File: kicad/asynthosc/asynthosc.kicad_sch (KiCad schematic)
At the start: 14 parts

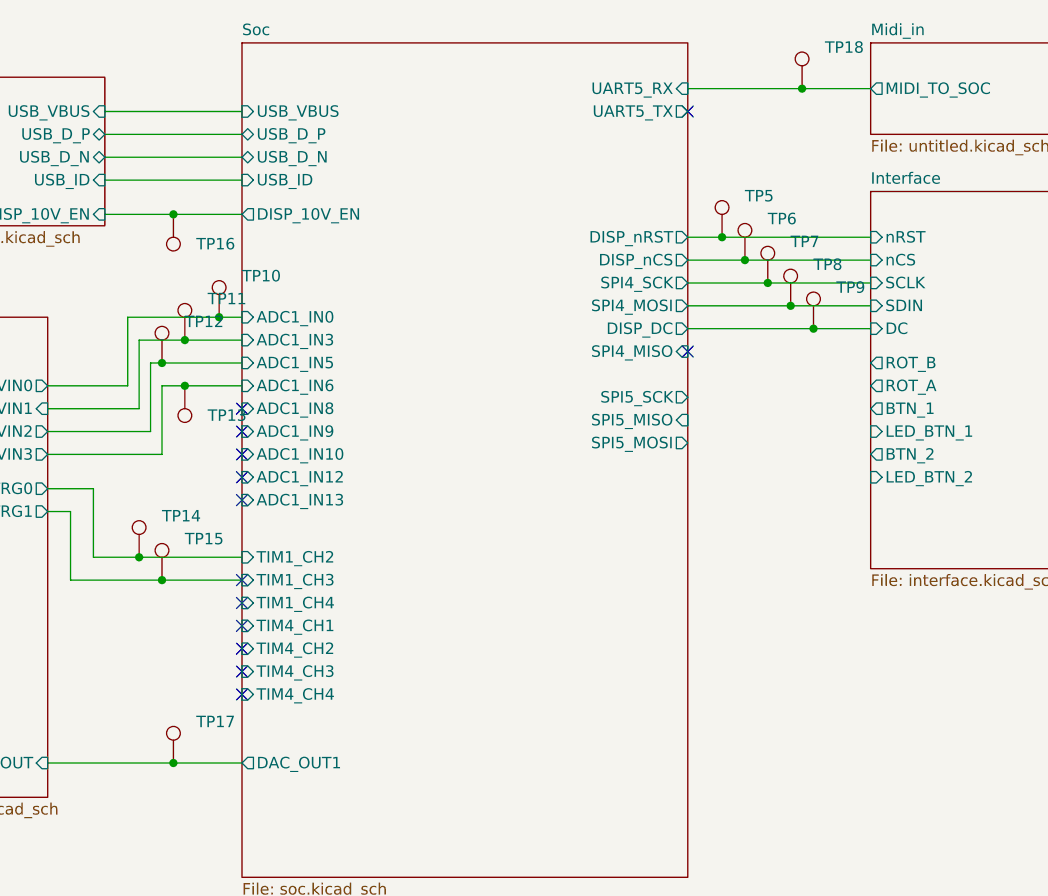
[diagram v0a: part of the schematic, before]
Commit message: pcb: place and change some components for easier routing
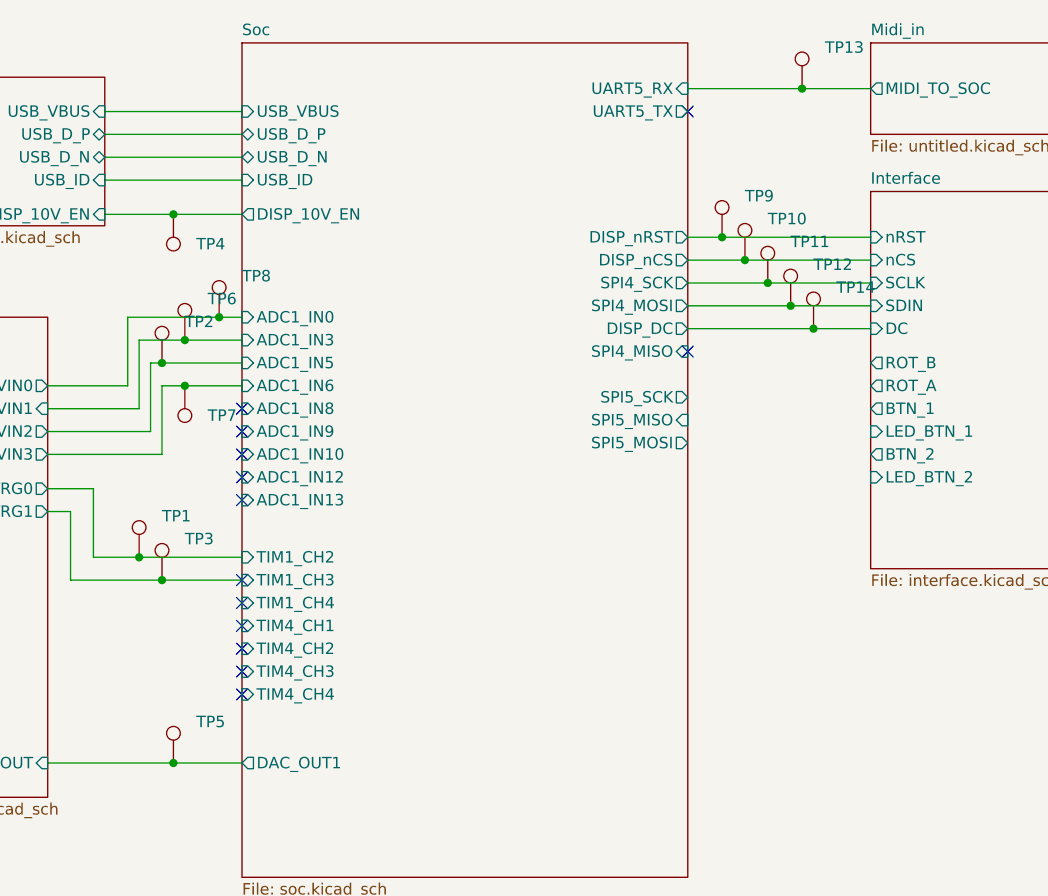
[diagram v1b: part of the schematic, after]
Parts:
- renumbered TP14 to TP1, TP6 to TP10, TP7 to TP11, TP8 to TP12, TP18 to TP13, TP9 to TP14, TP12 to TP2, TP15 to TP3, TP16 to TP4, TP17 to TP5, TP11 to TP6, TP13 to TP7, TP10 to TP8, TP5 to TP9
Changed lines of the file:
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@@
 		(dnp no)
 		(fields_autoplaced yes)
-		(property "Reference" "TP10"
+		(property "Reference" "TP8"
 			(at 127 97.0279 0)
 			(effects
@@
 			(project "asynthosc"
 				(path "/d73e377a-a016-415f-8824-91cc6e4907b9"
-					(reference "TP10")
+					(reference "TP8")
 					(unit 1)
 				)
@@
 		(dnp no)
 		(fields_autoplaced yes)
-		(property "Reference" "TP8"
+		(property "Reference" "TP12"
 			(at 190.5 95.7579 0)
 			(effects
@@
 			(project "asynthosc"
 				(path "/d73e377a-a016-415f-8824-91cc6e4907b9"
-					(reference "TP8")
+					(reference "TP12")
 					(unit 1)
 				)
@@
 		(dnp no)
 		(fields_autoplaced yes)
-		(property "Reference" "TP7"
+		(property "Reference" "TP11"
 			(at 187.96 93.2179 0)
 			(effects
@@
 			(project "asynthosc"
 				(path "/d73e377a-a016-415f-8824-91cc6e4907b9"
-					(reference "TP7")
+					(reference "TP11")
 					(unit 1)
 				)
@@
 		(dnp no)
 		(fields_autoplaced yes)
-		(property "Reference" "TP15"
+		(property "Reference" "TP3"
 			(at 120.65 126.2379 0)
 			(effects
@@
 			(project "asynthosc"
 				(path "/d73e377a-a016-415f-8824-91cc6e4907b9"
-					(reference "TP15")
+					(reference "TP3")
 					(unit 1)
 				)
@@
 		(dnp no)
 		(fields_autoplaced yes)
-		(property "Reference" "TP14"
+		(property "Reference" "TP1"
 			(at 118.11 123.6979 0)
 			(effects
@@
 			(project "asynthosc"
 				(path "/d73e377a-a016-415f-8824-91cc6e4907b9"
-					(reference "TP14")
+					(reference "TP1")
 					(unit 1)
 				)
@@
 		(dnp no)
 		(fields_autoplaced yes)
-		(property "Reference" "TP17"
+		(property "Reference" "TP5"
 			(at 121.92 146.5579 0)
 			(effects
@@
 			(project "asynthosc"
 				(path "/d73e377a-a016-415f-8824-91cc6e4907b9"
-					(reference "TP17")
+					(reference "TP5")
 					(unit 1)
 				)
@@
 		(dnp no)
 		(fields_autoplaced yes)
-		(property "Reference" "TP13"
+		(property "Reference" "TP7"
 			(at 123.19 112.5219 0)
 			(effects
@@
 			(project "asynthosc"
 				(path "/d73e377a-a016-415f-8824-91cc6e4907b9"
-					(reference "TP13")
+					(reference "TP7")
 					(unit 1)
 				)
@@
 		(dnp no)
 		(fields_autoplaced yes)
-		(property "Reference" "TP16"
+		(property "Reference" "TP4"
 			(at 121.92 93.4719 0)
 			(effects
@@
 			(project "asynthosc"
 				(path "/d73e377a-a016-415f-8824-91cc6e4907b9"
-					(reference "TP16")
+					(reference "TP4")
 					(unit 1)
 				)
@@
 		(dnp no)
 		(fields_autoplaced yes)
-		(property "Reference" "TP5"
+		(property "Reference" "TP9"
 			(at 182.88 88.1379 0)
 			(effects
@@
 			(project "asynthosc"
 				(path "/d73e377a-a016-415f-8824-91cc6e4907b9"
-					(reference "TP5")
+					(reference "TP9")
 					(unit 1)
 				)
@@
 		(dnp no)
 		(fields_autoplaced yes)
-		(property "Reference" "TP12"
+		(property "Reference" "TP2"
 			(at 120.65 102.1079 0)
 			(effects
@@
 			(project "asynthosc"
 				(path "/d73e377a-a016-415f-8824-91cc6e4907b9"
-					(reference "TP12")
+					(reference "TP2")
 					(unit 1)
 				)
@@
 		(dnp no)
 		(fields_autoplaced yes)
-		(property "Reference" "TP11"
+		(property "Reference" "TP6"
 			(at 123.19 99.5679 0)
 			(effects
@@
 			(project "asynthosc"
 				(path "/d73e377a-a016-415f-8824-91cc6e4907b9"
-					(reference "TP11")
+					(reference "TP6")
 					(unit 1)
 				)
@@
 		(dnp no)
 		(fields_autoplaced yes)
-		(property "Reference" "TP18"
+		(property "Reference" "TP13"
 			(at 191.77 71.6279 0)
 			(effects
@@
 			(project "asynthosc"
 				(path "/d73e377a-a016-415f-8824-91cc6e4907b9"
-					(reference "TP18")
+					(reference "TP13")
 					(unit 1)
 				)
@@
 		(dnp no)
 		(fields_autoplaced yes)
-		(property "Reference" "TP9"
+		(property "Reference" "TP14"
 			(at 193.04 98.2979 0)
 			(effects
@@
 			(project "asynthosc"
 				(path "/d73e377a-a016-415f-8824-91cc6e4907b9"
-					(reference "TP9")
+					(reference "TP14")
 					(unit 1)
 				)
@@
 		(dnp no)
 		(fields_autoplaced yes)
-		(property "Reference" "TP6"
+		(property "Reference" "TP10"
 			(at 185.42 90.6779 0)
 			(effects
@@
 			(project "asynthosc"
 				(path "/d73e377a-a016-415f-8824-91cc6e4907b9"
-					(reference "TP6")
-					(unit 1)
-				)
+					(reference "TP10")
+					(unit 1)
+				)

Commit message: pcb: place and draft route
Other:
- sheet Soc ports: added UART4_RX, UART4_TX; removed ADC1_IN10, ADC1_IN12, ADC1_IN13, SPI5_MISO, SPI5_MOSI, SPI5_SCK, TIM1_CH2, TIM1_CH4, TIM4_CH1, TIM4_CH2, TIM4_CH3, TIM4_CH4, UART5_RX, UART5_TX
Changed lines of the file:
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@@
-			)
-		)
-		(pin "ADC1_IN10" input
-			(at 127 116.84 180)
-			(effects
-				(font
-					(size 1.27 1.27)
-				)
-				(justify left)
-			)
-		)
-		(pin "ADC1_IN12" input
-			(at 127 119.38 180)
-			(effects
-				(font
-					(size 1.27 1.27)
-				)
-				(justify left)
-			)
-		)
-		(pin "ADC1_IN13" input
-			(at 127 121.92 180)
-			(effects
-				(font
-					(size 1.27 1.27)
-				)
-				(justify left)
-			)
-		)
-		(pin "TIM1_CH2" input
-			(at 127 128.27 180)
-			(effects
-				(font
-					(size 1.27 1.27)
-				)
-				(justify left)
-			)
-		)
-		(pin "TIM1_CH4" input
-			(at 127 133.35 180)
-			(effects
-				(font
-					(size 1.27 1.27)
-				)
-				(justify left)
 			)
 		)
@@
 				)
 				(justify left)
-			)
-		)
-		(pin "TIM4_CH1" input
-			(at 127 135.89 180)
-			(effects
-				(font
-					(size 1.27 1.27)
-				)
-				(justify left)
-			)
-		)
-		(pin "TIM4_CH2" input
-			(at 127 138.43 180)
-			(effects
-				(font
-					(size 1.27 1.27)
-				)
-				(justify left)
-			)
-		)
-		(pin "TIM4_CH3" input
-			(at 127 140.97 180)
-			(effects
-				(font
-					(size 1.27 1.27)
-				)
-				(justify left)
-			)
-		)
-		(pin "TIM4_CH4" input
-			(at 127 143.51 180)
-			(effects
-				(font
-					(size 1.27 1.27)
-				)
-				(justify left)
-			)
-		)
-		(pin "UART5_RX" input
-			(at 176.53 76.2 0)
-			(effects
-				(font
-					(size 1.27 1.27)
-				)
-				(justify right)
-			)
-		)
-		(pin "UART5_TX" output
-			(at 176.53 78.74 0)
-			(effects
-				(font
-					(size 1.27 1.27)
-				)
-				(justify right)
 			)
 		)
@@
 			)
 		)
-		(pin "SPI5_SCK" output
-			(at 176.53 110.49 0)
+		(pin "DISP_nCS" output
+			(at 176.53 95.25 0)
 			(effects
 				(font
@@
 			)
 		)
-		(pin "SPI5_MISO" input
-			(at 176.53 113.03 0)
+		(pin "UART4_TX" output
+			(at 176.53 78.74 0)
 			(effects
 				(font
@@
 			)
 		)
-		(pin "SPI5_MOSI" output
-			(at 176.53 115.57 0)
+		(pin "UART4_RX" input
+			(at 176.53 76.2 0)
 			(effects
 				(font
-					(size 1.27 1.27)
-				)
-				(justify right)
-			)
-		)
-		(pin "DISP_nCS" output
-			(at 176.53 95.25 0)
-			(effects
-				(font

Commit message: pcb: routing
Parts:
- added TP24, TP25: TestPoint, TestPoint:TestPoint_Pad_D1.0mm, symbol Connector:TestPoint
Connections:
- net Soc/SPI4_MISO: now also TP24.1
- new net Soc/DISP_12V_EN: TP25.1
- no-connect marks 13 -> 3
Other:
- sheet Soc ports: added BTN_1, BTN_2, DISP_12V_EN, LED_BTN_1, LED_BTN_2, ROT_A, ROT_B, TIM15_CH1, TIM15_CH2, TIM1_CH1, TIM1_CH4; removed none
- sheet Supply ports: added DISP_12V_EN; removed none
- moved on the sheet: TP1, TP3, TP4

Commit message: sch: pcb: tiny fixes and changes
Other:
- sheet Supply ports: added VBUS; removed USB_VBUS
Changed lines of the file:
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@@
-			)
-		)
-		(pin "USB_VBUS" input
-			(at 111.76 78.74 0)
-			(effects
-				(font
-					(size 1.27 1.27)
-				)
-				(justify right)
 			)
 		)
@@
 		(pin "DISP_12V_EN" input
 			(at 111.76 92.71 0)
+			(effects
+				(font
+					(size 1.27 1.27)
+				)
+				(justify right)
+			)
+		)
+		(pin "VBUS" output
+			(at 111.76 78.74 0)
 			(effects
 				(font
@@
 	(sheet
 		(at 196.85 87.63)
-		(size 25.4 41.91)
+		(size 25.4 55.88)
 		(fields_autoplaced yes)
 		(stroke
@@
 		)
 		(property "Sheetfile" "interface.kicad_sch"
-			(at 196.85 130.1246 0)
+			(at 196.85 144.0946 0)
 			(effects
 				(font

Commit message: sch: pcb: wip and silkscreen cleaning
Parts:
- added TP31, TP32: TestPoint, TestPoint:TestPoint_Pad_D1.0mm, symbol Connector:TestPoint
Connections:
- net Soc/ADC1_IN9: now also TP31.1
- net Soc/UART4_TX: now also TP32.1
- no-connect marks 3 -> 0
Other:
- sheet Soc ports: added none; removed ADC1_IN8, TIM15_CH1, TIM15_CH2, TIM1_CH1
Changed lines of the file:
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@@
 		(color 0 0 0 0)
 	)
-	(no_connect
-		(at 127 114.3)
-	)
-	(no_connect
-		(at 127 111.76)
-	)
-	(no_connect
-		(at 176.53 78.74)
-	)
 	(wire
 		(pts
@@
 	(wire
 		(pts
+			(xy 120.65 114.3) (xy 127 114.3)
+		)
+		(stroke
+			(width 0)
+			(type default)
+		)
+	)
+	(wire
+		(pts
 			(xy 115.57 104.14) (xy 120.65 104.14)
 		)
@@
 		(pts
 			(xy 115.57 111.76) (xy 115.57 104.14)
+		)
+		(stroke
+			(width 0)
+			(type default)
+		)
+	)
+	(wire
+		(pts
+			(xy 176.53 78.74) (xy 180.34 78.74)
 		)
 		(stroke
@@
 	(symbol
 		(lib_id "Connector:TestPoint")
+		(at 180.34 78.74 180)
+		(unit 1)
+		(exclude_from_sim yes)
+		(in_bom yes)
+		(on_board yes)
+		(dnp no)
+		(fields_autoplaced yes)
+		(property "Reference" "TP32"
+			(at 182.88 82.0419 0)
+			(effects
+				(font
+					(size 1.27 1.27)
+				)
+				(justify right)
+			)
+		)
+		(property "Value" "TestPoint"
+			(at 177.8 80.7721 0)
+			(effects
+				(font
+					(size 1.27 1.27)
+				)
+				(justify left)
+				(hide yes)
+			)
+		)
+		(property "Footprint" "TestPoint:TestPoint_Pad_D1.0mm"
+			(at 175.26 78.74 0)
+			(effects
+				(font
+					(size 1.27 1.27)
+				)
+				(hide yes)
+			)
+		)
+		(property "Datasheet" "~"
+			(at 175.26 78.74 0)
+			(effects
+				(font
+					(size 1.27 1.27)
+				)
+				(hide yes)
+			)
+		)
+		(property "Description" "test point"
+			(at 180.34 78.74 0)
+			(effects
+				(font
+					(size 1.27 1.27)
+				)
+				(hide yes)
+			)
+		)
+		(property "LCSC" ""
+			(at 180.34 78.74 0)
+			(effects
+				(font
+					(size 1.27 1.27)
+				)
+				(hide yes)
+			)
+		)
+		(property "Manufacturer" ""
+			(at 180.34 78.74 0)
+			(effects
+				(font
+					(size 1.27 1.27)
+				)
+				(hide yes)
+			)
+		)
+		(property "RefNum" "_na_"
+			(at 180.34 78.74 0)
+			(effects
+				(font
+					(size 1.27 1.27)
+				)
+				(hide yes)
+			)
+		)
+		(pin "1"
+		)
+		(instances
+			(project "asynthosc"
+				(path "/d73e377a-a016-415f-8824-91cc6e4907b9"
+					(reference "TP32")
+					(unit 1)
+				)
+			)
+		)
+	)
+	(symbol
+		(lib_id "Connector:TestPoint")
 		(at 114.3 90.17 180)
 		(unit 1)
@@
 				(path "/d73e377a-a016-415f-8824-91cc6e4907b9"
 					(reference "TP4")
+					(unit 1)
+				)
+			)
+		)
+	)
+	(symbol
+		(lib_id "Connector:TestPoint")
+		(at 120.65 114.3 180)
+		(unit 1)
+		(exclude_from_sim yes)
+		(in_bom yes)
+		(on_board yes)
+		(dnp no)
+		(fields_autoplaced yes)
+		(property "Reference" "TP31"
+			(at 123.19 117.6019 0)
+			(effects
+				(font
+					(size 1.27 1.27)
+				)
+				(justify right)
+			)
+		)
+		(property "Value" "TestPoint"
+			(at 118.11 116.3321 0)
+			(effects
+				(font
+					(size 1.27 1.27)
+				)
+				(justify left)
+				(hide yes)
+			)
+		)
+		(property "Footprint" "TestPoint:TestPoint_Pad_D1.0mm"
+			(at 115.57 114.3 0)
+			(effects
+				(font
+					(size 1.27 1.27)
+				)
+				(hide yes)
+			)
+		)
+		(property "Datasheet" "~"
+			(at 115.57 114.3 0)
+			(effects
+				(font
+					(size 1.27 1.27)
+				)
+				(hide yes)
+			)
+		)
+		(property "Description" "test point"
+			(at 120.65 114.3 0)
+			(effects
+				(font
+					(size 1.27 1.27)
+				)
+				(hide yes)
+			)
+		)
+		(property "LCSC" ""
+			(at 120.65 114.3 0)
+			(effects
+				(font
+					(size 1.27 1.27)
+				)
+				(hide yes)
+			)
+		)
+		(property "Manufacturer" ""
+			(at 120.65 114.3 0)
+			(effects
+				(font
+					(size 1.27 1.27)
+				)
+				(hide yes)
+			)
+		)
+		(property "RefNum" "_na_"
+			(at 120.65 114.3 0)
+			(effects
+				(font
+					(size 1.27 1.27)
+				)
+				(hide yes)
+			)
+		)
+		(pin "1"
+		)
+		(instances
+			(project "asynthosc"
+				(path "/d73e377a-a016-415f-8824-91cc6e4907b9"
+					(reference "TP31")
 					(unit 1)
 				)
@@
 			)
 		)
-		(pin "ADC1_IN8" input
-			(at 127 111.76 180)
-			(effects
-				(font
-					(size 1.27 1.27)
-				)
-				(justify left)
-			)
-		)
 		(pin "ADC1_IN0" input
 			(at 127 101.6 180)
@@
 			(effects
 				(font
-					(size 1.27 1.27)
-				)
-				(justify right)
-			)
-		)
-		(pin "TIM1_CH1" input
-			(at 127 128.27 180)
-			(effects
-				(font
-					(size 1.27 1.27)
-				)
-				(justify left)
-			)
-		)
-		(pin "TIM15_CH2" input
-			(at 176.53 127 0)
-			(effects
-				(font
-					(size 1.27 1.27)
-				)
-				(justify right)
-			)
-		)
-		(pin "TIM15_CH1" input
-			(at 176.53 129.54 0)
-			(effects
-				(font

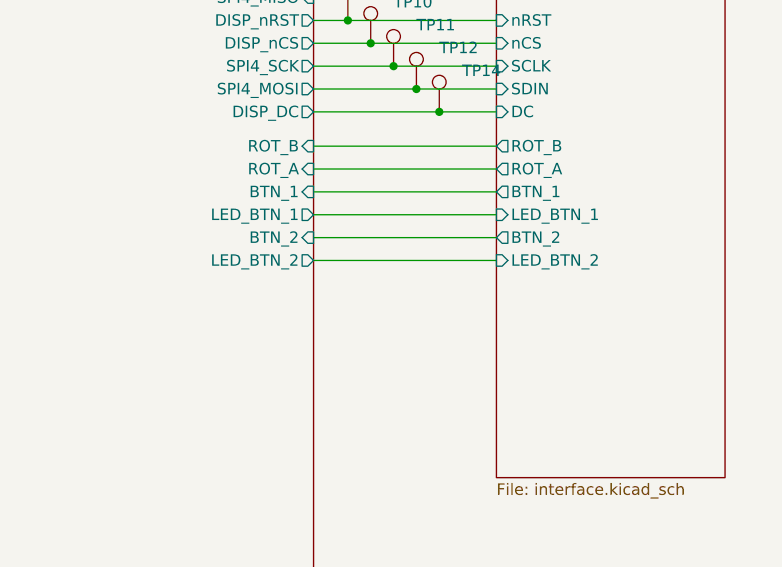
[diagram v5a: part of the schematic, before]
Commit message: sch: pcb: fix: footprint mismatches
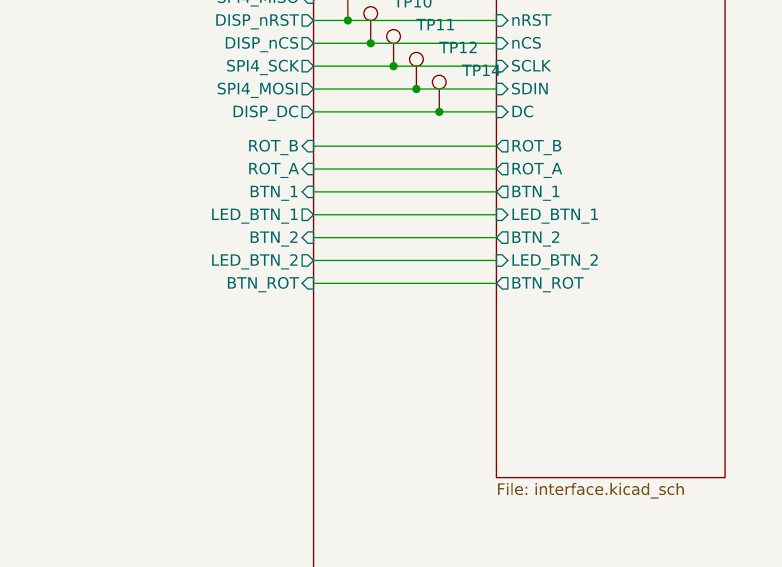
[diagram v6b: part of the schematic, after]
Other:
- sheet Interface ports: added BTN_ROT; removed none
- sheet Soc ports: added BTN_ROT; removed none
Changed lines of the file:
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@@
+	(wire
+		(pts
+			(xy 176.53 121.92) (xy 196.85 121.92)
+		)
+		(stroke
+			(width 0)
+			(type default)
+		)
+	)
 	(wire
 		(pts
@@
 			)
 		)
+		(pin "BTN_ROT" output
+			(at 196.85 121.92 180)
+			(effects
+				(font
+					(size 1.27 1.27)
+				)
+				(justify left)
+			)
+		)
 		(instances
 			(project "asynthosc"
@@
 			)
 		)
+		(pin "BTN_ROT" input
+			(at 176.53 121.92 0)
+			(effects
+				(font
+					(size 1.27 1.27)
+				)
+				(justify right)
+			)
+		)

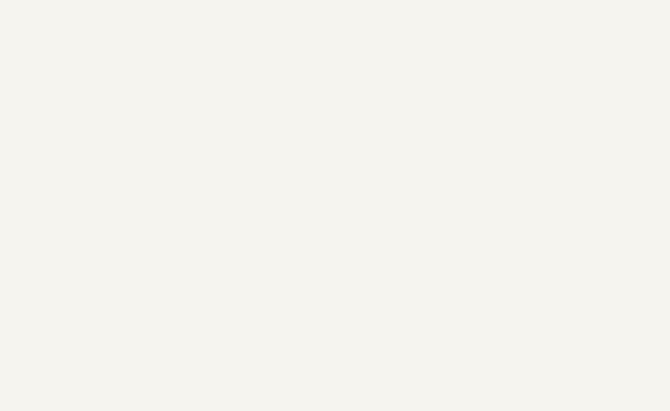
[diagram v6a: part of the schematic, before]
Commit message: pcb: sch: panel: add panelisation for pcba assembly
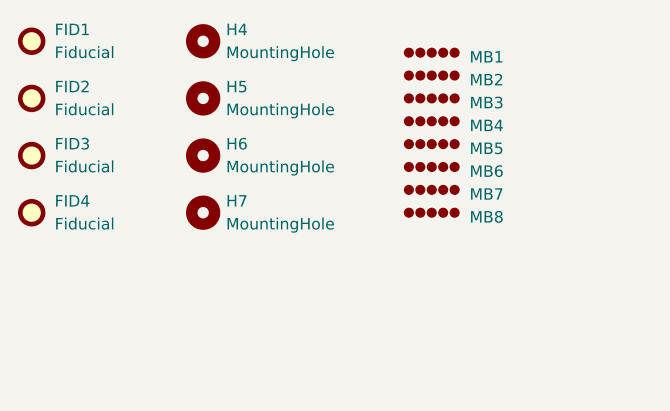
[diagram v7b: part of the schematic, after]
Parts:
- added FID1, FID2, FID3, FID4: Fiducial, Fiducial:Fiducial_1mm_Mask2mm, symbol Mechanical:Fiducial
- added H4, H5, H6, H7: MountingHole, asynthosc:MountingHole_JLC_3.5mm, symbol Mechanical:MountingHole
- added MB1, MB2, MB3, MB4, MB5, MB6, MB7, MB8: MouseBytes, asynthosc:MouseBytes_JLC, symbol asynthosc_lib:MouseBytes
